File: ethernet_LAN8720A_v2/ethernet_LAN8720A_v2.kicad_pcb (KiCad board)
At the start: 2 copper layers, 55.2 x 65.4 mm, 48 parts, among them P1 SI-52003-F, P3 PoE, U1 LAN8720A-CP, U2 ASV-50.000MHZ-E-T

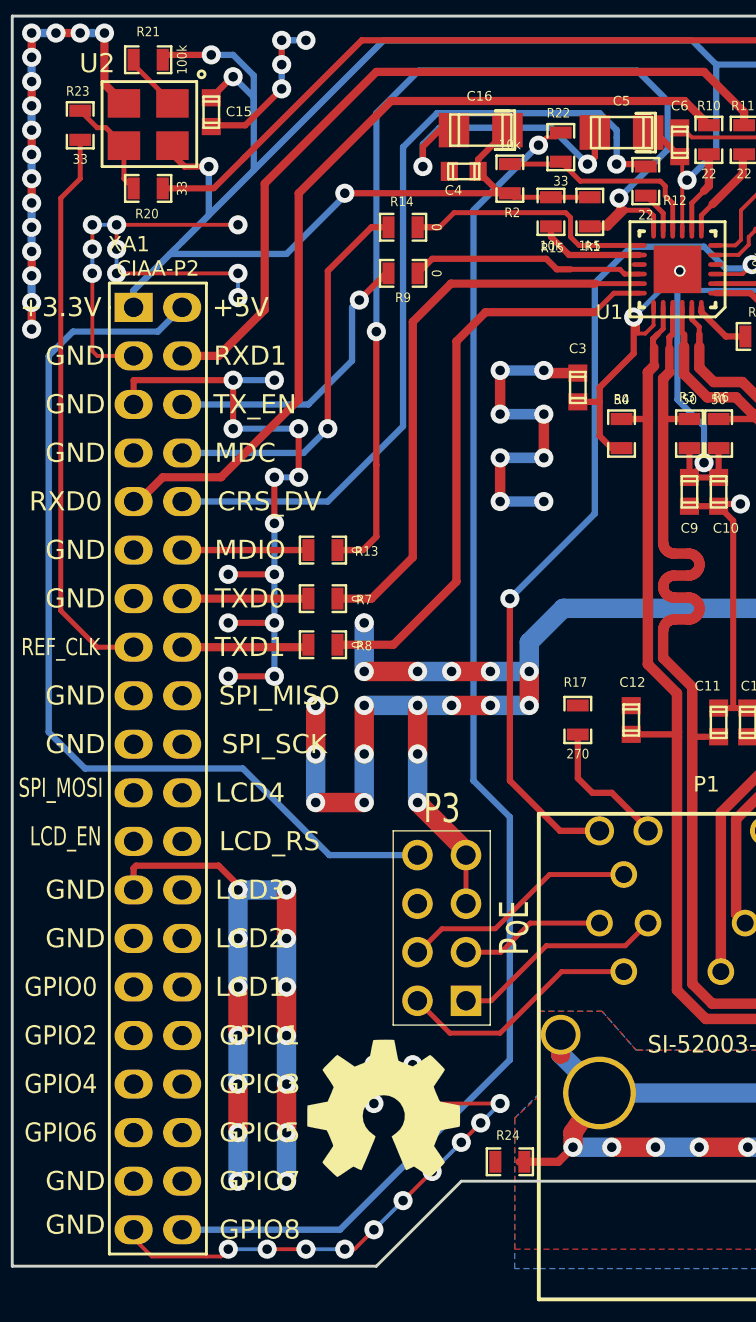
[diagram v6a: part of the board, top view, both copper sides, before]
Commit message: Agrego JP1. Agrego pullup a línea de reset.
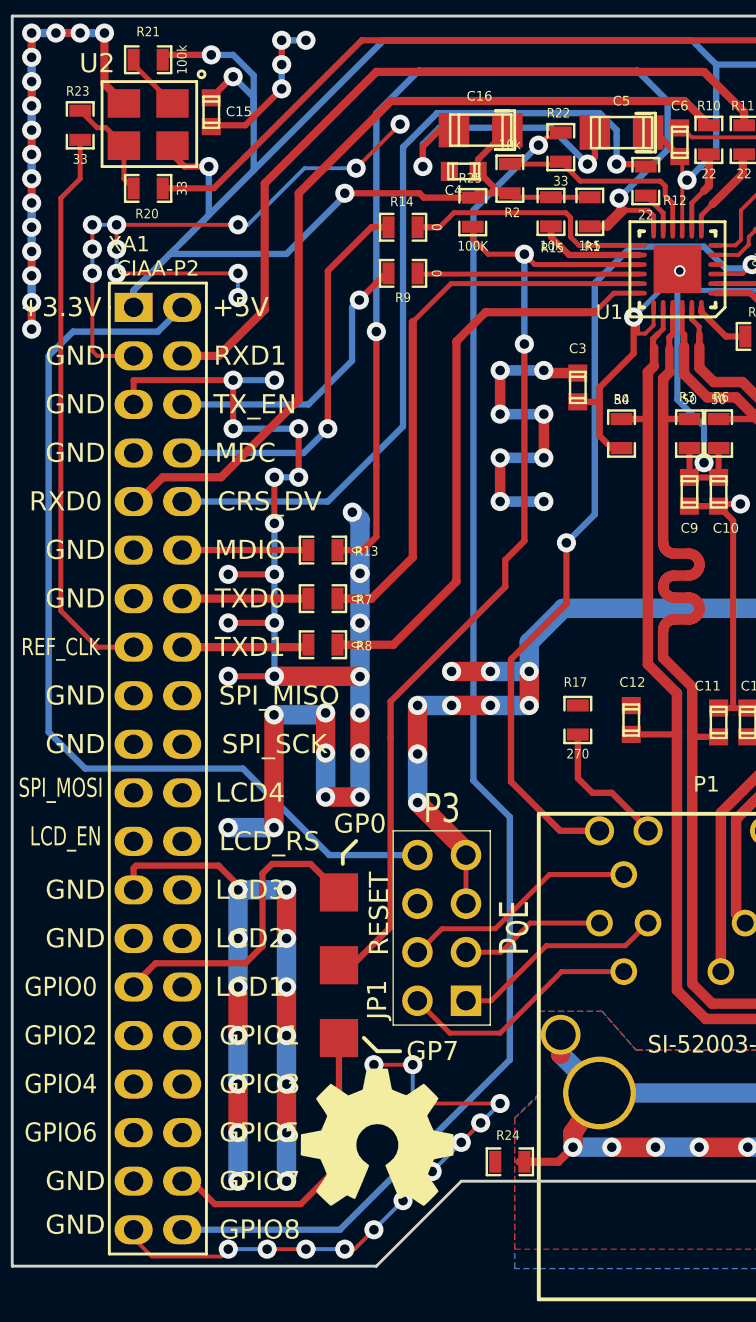
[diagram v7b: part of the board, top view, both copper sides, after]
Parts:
- added JP1: JUMPER3, Oddities:NetTie-II_SMD, F.Cu at (108.3, 118.4)
- added R25: 100K, eth:SM0603_Resistor, F.Cu at (115.3, 79.0)
- moved G101 1.55 mm to (110.3, 127.4)
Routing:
- net /Circuito Principal/PHY_nRESET: track 0.00 -> 51.7 mm, vias 0 -> 2
- net GND: track 345.9 -> 370.8 mm, vias 120 -> 126
- net /Circuito Principal/GPIO0: track 0.00 -> 17.0 mm
- net /Circuito Principal/GPIO7: track 0.00 -> 16.2 mm
- net /Circuito Principal/LED_LINK: track 45.3 -> 46.0 mm
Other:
- board text added: "GP0"
- board text added: "GP7"
- board text added: "RESET"

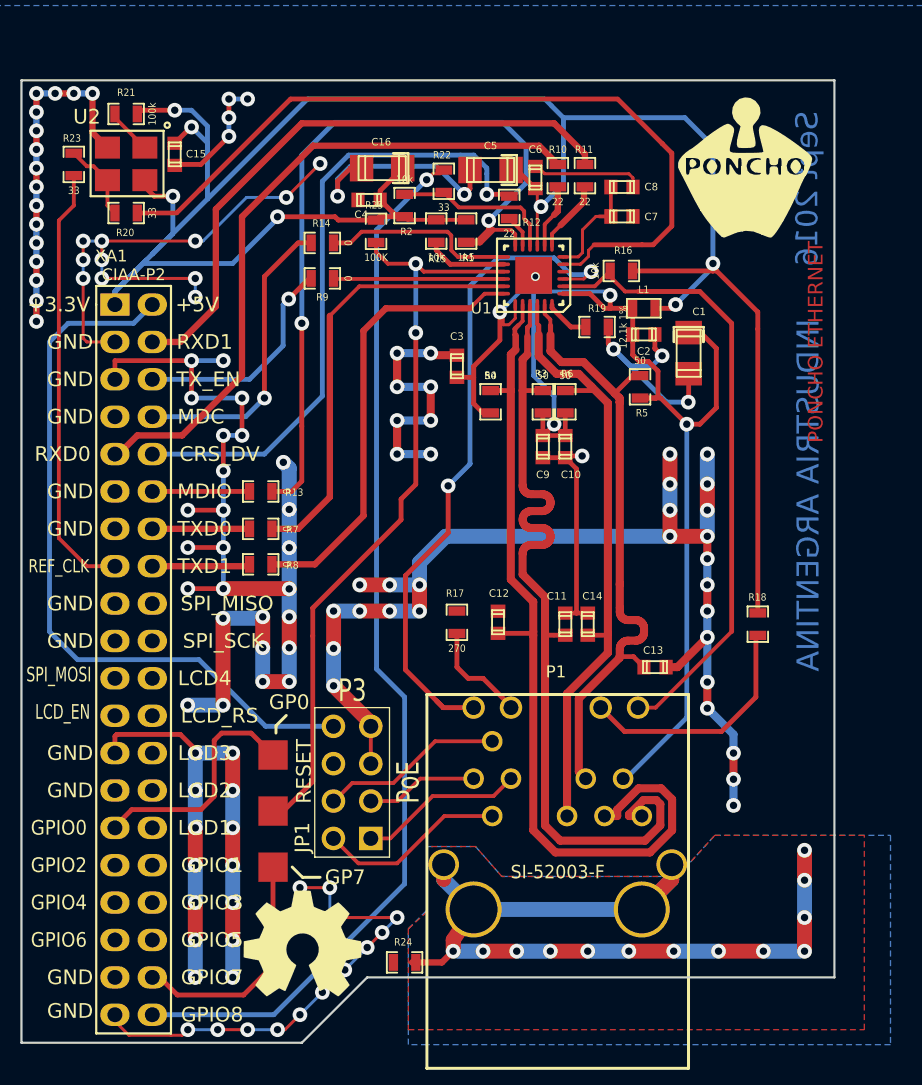
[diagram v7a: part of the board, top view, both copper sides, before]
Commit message: Agrego fiduciales y agujeros al PCB. Configuro DRC. Agrando vía debajo del IC, quito errores de DRC, reorganizo textos.
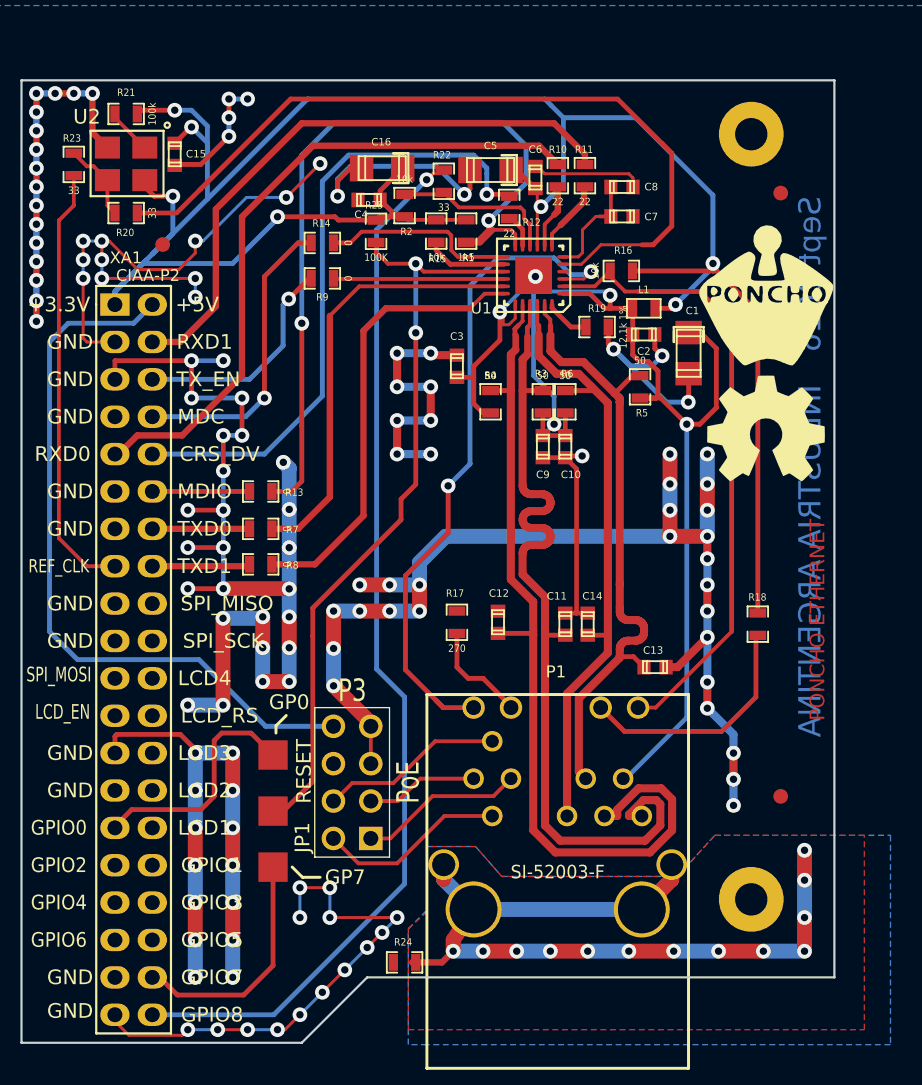
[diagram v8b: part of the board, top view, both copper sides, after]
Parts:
- added FID1: FIDUCIAL, eth:Fiducial_1mm_Dia_2.54mm_Outer_CopperTop, F.Cu at (142.8, 117.4)
- added FID2: FIDUCIAL, eth:Fiducial_1mm_Dia_2.54mm_Outer_CopperTop, F.Cu at (142.8, 76.4)
- added FID3: FIDUCIAL, eth:Fiducial_1mm_Dia_2.54mm_Outer_CopperTop, F.Cu at (100.8, 79.9)
- added MH1: MOUNTING-HOLE, eth:MountingHole_2.2mm_M2_Pad, F.Cu at (140.8, 124.4)
- added MH2: MOUNTING-HOLE, eth:MountingHole_2.2mm_M2_Pad, F.Cu at (140.8, 72.4)
- moved G101 47.1 mm to (141.8, 92.4)
- moved G*** 8.81 mm to (141.8, 83.4)
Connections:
- P3 pad 6: Net-(P3-Pad6) -> (no net)
- U1 pad 4: Net-(U1-Pad4) -> (no net)
- XA1 pad 58: /Circuito Principal/MISO -> (no net)
- XA1 pad 60: /Circuito Principal/spiSCK -> (no net)
- XA1 pad 61: /Circuito Principal/MOSI -> (no net)
- XA1 pad 62: /Circuito Principal/LCD4 -> (no net)
- XA1 pad 63: /Circuito Principal/LCD_EN -> (no net)
- XA1 pad 64: /Circuito Principal/RS -> (no net)
- XA1 pad 66: /Circuito Principal/LCD3 -> (no net)
- XA1 pad 68: /Circuito Principal/LCD2 -> (no net)
- XA1 pad 70: /Circuito Principal/LCD1 -> (no net)
- XA1 pad 71: /Circuito Principal/GPIO2 -> (no net)
- XA1 pad 72: /Circuito Principal/GPIO1 -> (no net)
- XA1 pad 73: /Circuito Principal/GPIO4 -> (no net)
- XA1 pad 74: /Circuito Principal/GPIO3 -> (no net)
- XA1 pad 75: /Circuito Principal/GPIO6 -> (no net)
- XA1 pad 76: /Circuito Principal/GPIO5 -> (no net)
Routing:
- net GND: track 370.8 -> 372.8 mm
- net +3.3V: track 159.6 -> 157.6 mm
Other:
- net class Default: trace_width 0.33 -> 0.2; via_dia 0.6 -> 0.8
- rule via_min_drill: 0.3 -> 0.4
- rule via_min_size: 0.4 -> 0.8
- board text added: "Capas cobre: 2 Espesor placa: 1,6 mm. Espesor de Cobre: 1 Oz. Soporte: FR4 Estándar de Fabricación: Mayer de 8 MILS. Ver: http://www.mayerpcb.com/uploads/estandares.pdf"
- board text removed: "*Falta asociar footprint del jumper de 3 posiciones."
- board text removed: "Diseño simple faz. Sin requerimientos especiales."
- board text removed: "Editar el stackup para reflejar cantidad de capas, si se han realizado cálculos de impedancia o si es relevante para el funcionamiento."
